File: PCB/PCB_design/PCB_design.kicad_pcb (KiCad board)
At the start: 2 copper layers, 68.2 x 66 mm, 55 parts, among them J1 Conn_01x01_Pin, J2 Conn_01x01_Pin, J3 Conn_01x01_Pin, J4 Conn_01x01_Pin, J5 Conn_01x01_Pin, J6 Conn_01x01_Pin, J7 Conn_02x04_Counter_Clockwise, J8 Conn_01x01_Pin, K1 Relay_SPST-NO, K2 Relay_SPST-NO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

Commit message: Regroupement partie AC
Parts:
- moved J1 50.5 mm to (145.9, 37.9), turned to 180 degrees
- moved J8 35.5 mm to (134.9, 37.6), turned to 180 degrees
- moved R11 32.6 mm to (102.2, 84.4), turned to 0 degrees
- moved F1 32.5 mm to (131.6, 43.9), turned to 180 degrees
- moved J2 31.2 mm to (128.3, 37.6), turned to 180 degrees
- moved R10 27.3 mm to (108.2, 88.7)
- moved R4 26.6 mm to (102.8, 79.8), turned to 180 degrees
- moved C9 24.5 mm to (107.0, 80.8), turned to -90 degrees
- moved R5 22.1 mm to (108.2, 86.2)
- moved U3 20.2 mm to (112.3, 81.8)
- moved R7 19.5 mm to (102.8, 74.5)
- moved D3 18.8 mm to (102.8, 68.5), turned to -90 degrees
- moved C1 18.6 mm to (121.9, 46.0), turned to 90 degrees
- moved C8 17.2 mm to (116.5, 87.9)
- moved D2 17.2 mm to (125.2, 73.9)
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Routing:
- net L: track 251.2 -> 279.2 mm, vias 14 -> 24
- net N: track 41.3 -> 18.3 mm
- net Net-(C1-Pad1): track 38.9 -> 16.3 mm
- net Net-(R11-Pad1): track 1.83 -> 24.3 mm, vias 0 -> 2
- net GND2: track 187.6 -> 208.9 mm, vias 1 -> 2
- net Net-(D1-+): track 14.3 -> 29.7 mm
- net Vaux: track 30.3 -> 16.0 mm
- net Net-(U3-FB): track 9.94 -> 23.5 mm
- net GND: track 109.9 -> 97.2 mm, vias 4 -> 1
- net Net-(D3-K): track 2.84 -> 15.3 mm
- net Net-(D4-A): track 34.5 -> 46.2 mm, vias 0 -> 1
- net VCC_IC: track 7.56 -> 12.3 mm
- net C: track 33.2 -> 34.5 mm
- net +310VDC: track 71.8 -> 70.7 mm, vias 1 -> 0
- net CT2: track 118.9 -> 118.4 mm
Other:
- board size 68.2 x 66 mm -> 64.3 x 77.8 mm

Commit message: J7 femelle
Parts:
- J7: footprint Connector_PinHeader_2.54mm:PinHeader_2x04_P2.54mm_Vertical -> Connector_PinSocket_2.54mm:PinSocket_2x04_P2.54mm_Vertical
- moved J7 2.28 mm to (122.7, 96.8)
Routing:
- net CT2: track 118.4 -> 135.9 mm
- net CT3: track 21.5 -> 27.6 mm, vias 0 -> 1
- net CT1: track 104.8 -> 99.5 mm
- net +5VDC: track 135.4 -> 138.9 mm
- net +3.3V: track 43.2 -> 40.4 mm
- net CT4: track 8.75 -> 6.27 mm
- net GND2: track 208.9 -> 207.3 mm

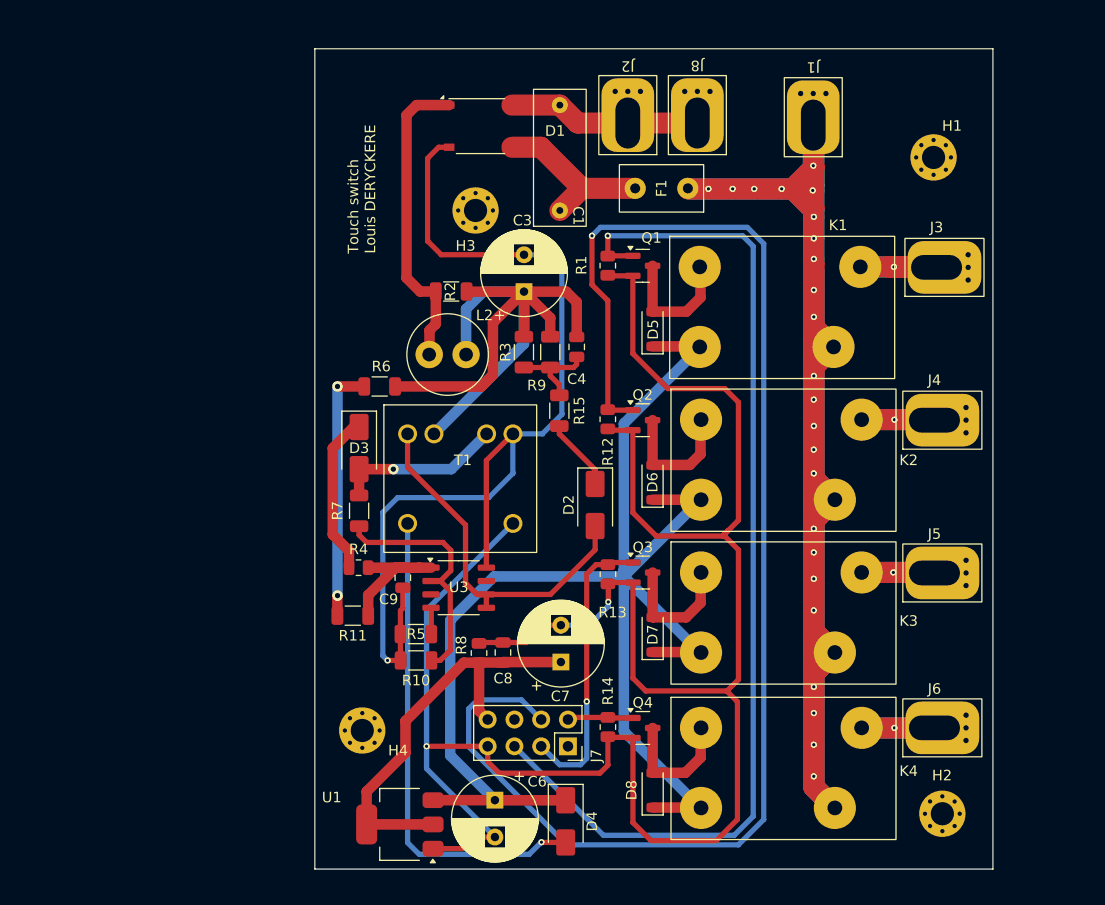
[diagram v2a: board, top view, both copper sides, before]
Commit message: Routage : séparation primaire/secondaire
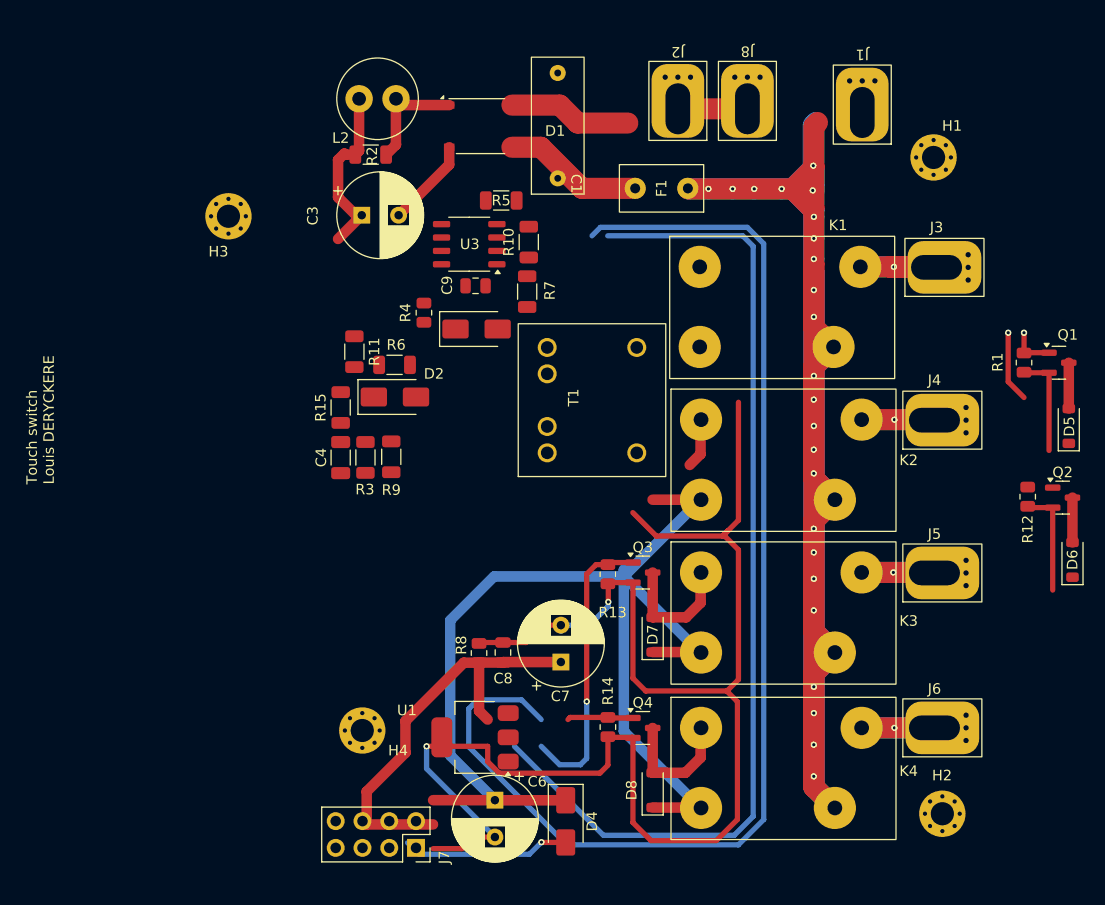
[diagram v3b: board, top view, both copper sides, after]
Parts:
- C4: footprint Capacitor_SMD:C_0805_2012Metric -> Capacitor_SMD:C_1206_3216Metric
- moved R5 41.9 mm to (116.3, 45.0), turned to 180 degrees
- moved R10 41.1 mm to (119.0, 49.0), turned to -90 degrees
- moved D5 40.6 mm to (170.2, 66.4)
- moved Q1 40.6 mm to (169.3, 60.4)
- moved R1 40.6 mm to (165.9, 60.4)
- moved Q2 40.5 mm to (169.6, 73.2)
- moved D6 40.5 mm to (170.6, 79.1)
- moved R12 40.5 mm to (166.3, 73.1)
- moved U3 32.6 mm to (113.3, 49.1), turned to 180 degrees
- moved C9 28.5 mm to (113.9, 53.1), turned to 180 degrees
- moved R7 26.2 mm to (118.8, 53.6), turned to 90 degrees
- moved R11 25.1 mm to (102.4, 59.4), turned to 90 degrees
- moved R4 25.0 mm to (109.0, 55.6), turned to -90 degrees
- moved C4 24.7 mm to (101.1, 69.4), turned to 90 degrees
- moved L2 24.5 mm to (106.3, 35.4), turned to 180 degrees
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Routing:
- net GND: track 97.2 -> 8.44 mm, vias 1 -> 0
- net +310VDC: track 70.7 -> 17.1 mm
- net GND2: track 207.3 -> 170.9 mm
- net C: track 34.5 -> 0.00 mm
- net Net-(D4-A): track 46.2 -> 15.9 mm
- net +5VDC: track 138.9 -> 110.2 mm
- net Net-(R11-Pad1): track 24.3 -> 0.00 mm, vias 2 -> 0
- net Net-(U3-FB): track 23.5 -> 0.00 mm
- net Net-(D1-+): track 29.7 -> 11.0 mm
- net Vaux: track 16.0 -> 0.00 mm, vias 1 -> 0
- net Net-(D3-K): track 15.3 -> 0.00 mm
- net CT2: track 135.9 -> 123.1 mm
- net VCC_IC: track 12.3 -> 0.00 mm
- net Net-(C4-Pad2): track 8.83 -> 0.00 mm
- net Net-(D5-A): track 12.4 -> 4.35 mm
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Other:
- board outline removed

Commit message: Routage
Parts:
- moved Q2 41.4 mm to (128.6, 79.2)
- moved Q1 41.4 mm to (128.4, 53.6)
- moved R12 41.3 mm to (125.5, 79.2)
- moved D5 40.1 mm to (131.7, 55.2)
- moved D6 38.7 mm to (131.8, 79.8)
- moved R1 37.5 mm to (128.6, 56.6), turned to 180 degrees
- moved H3 28.7 mm to (115.5, 32.5)
- moved C6 24.6 mm to (108.8, 78.3), turned to 0 degrees
- moved D4 22.9 mm to (119.8, 81.2), turned to 0 degrees
- moved J7 16.3 mm to (103.2, 90.9), turned to 0 degrees
- moved C7 12.5 mm to (111.2, 95.0), turned to -90 degrees
- moved H4 9.70 mm to (100.4, 104.6)
- moved U1 8.89 mm to (111.1, 87.5), turned to -90 degrees
- moved R8 6.95 mm to (119.2, 92.8), turned to 90 degrees
- moved Q3 5.83 mm to (128.5, 86.0)
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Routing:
- net CT2: track 123.1 -> 39.1 mm
- net GND2: track 170.9 -> 101.3 mm, vias 2 -> 4
- net GND: track 8.44 -> 63.8 mm, vias 0 -> 1
- net L: track 279.2 -> 225.5 mm, vias 24 -> 21
- net +310VDC: track 17.1 -> 58.5 mm, vias 0 -> 2
- net C: track 0.00 -> 38.8 mm, vias 0 -> 2
- net CT4: track 6.27 -> 35.4 mm, vias 0 -> 1
- net VCC_IC: track 0.00 -> 18.8 mm
- net CT1: track 99.5 -> 117.2 mm
- net Vaux: track 0.00 -> 11.9 mm
- net +3.3V: track 40.4 -> 52.0 mm
- net +5VDC: track 110.2 -> 120.0 mm, vias 0 -> 7
- net CT3: track 27.6 -> 35.8 mm
- net Net-(D6-A): track 8.98 -> 15.8 mm
- net Net-(D3-K): track 0.00 -> 6.73 mm
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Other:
- board outline added: 67.4 x 80 mm

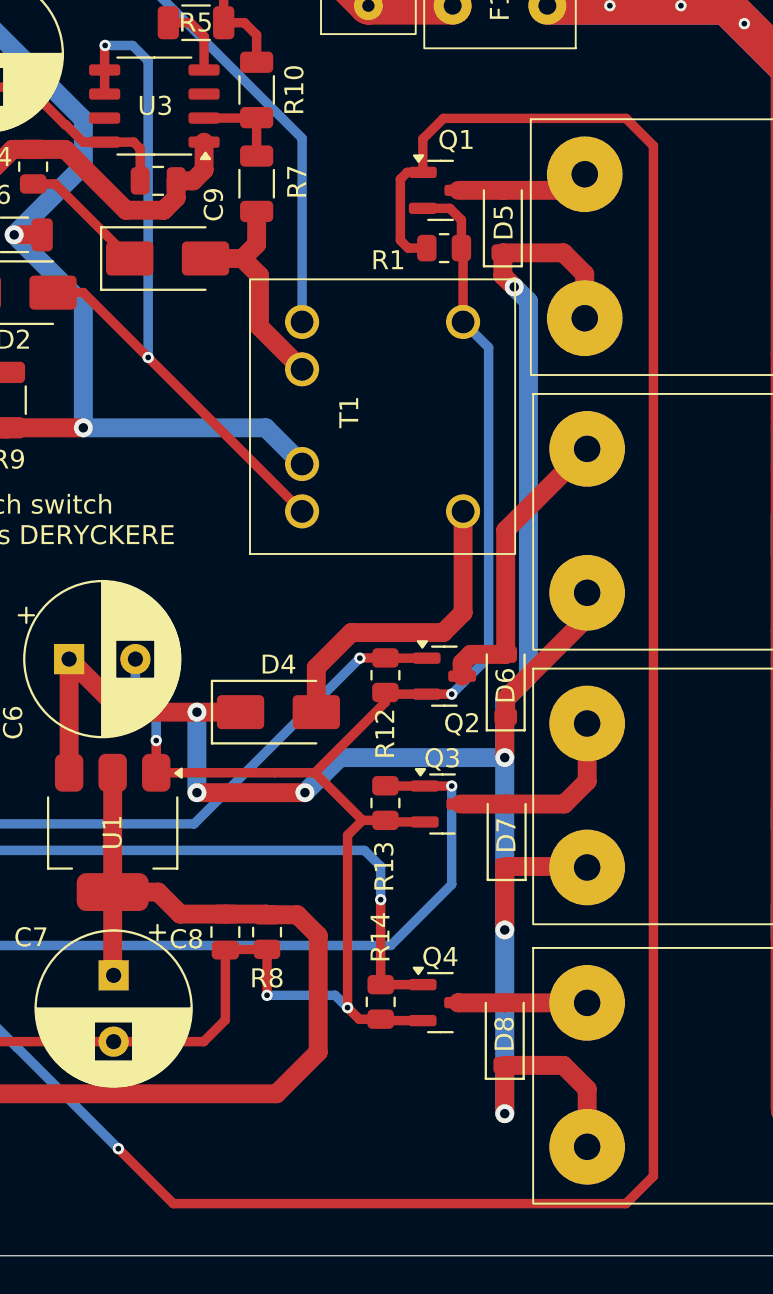
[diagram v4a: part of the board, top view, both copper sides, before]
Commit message: Rédaction README
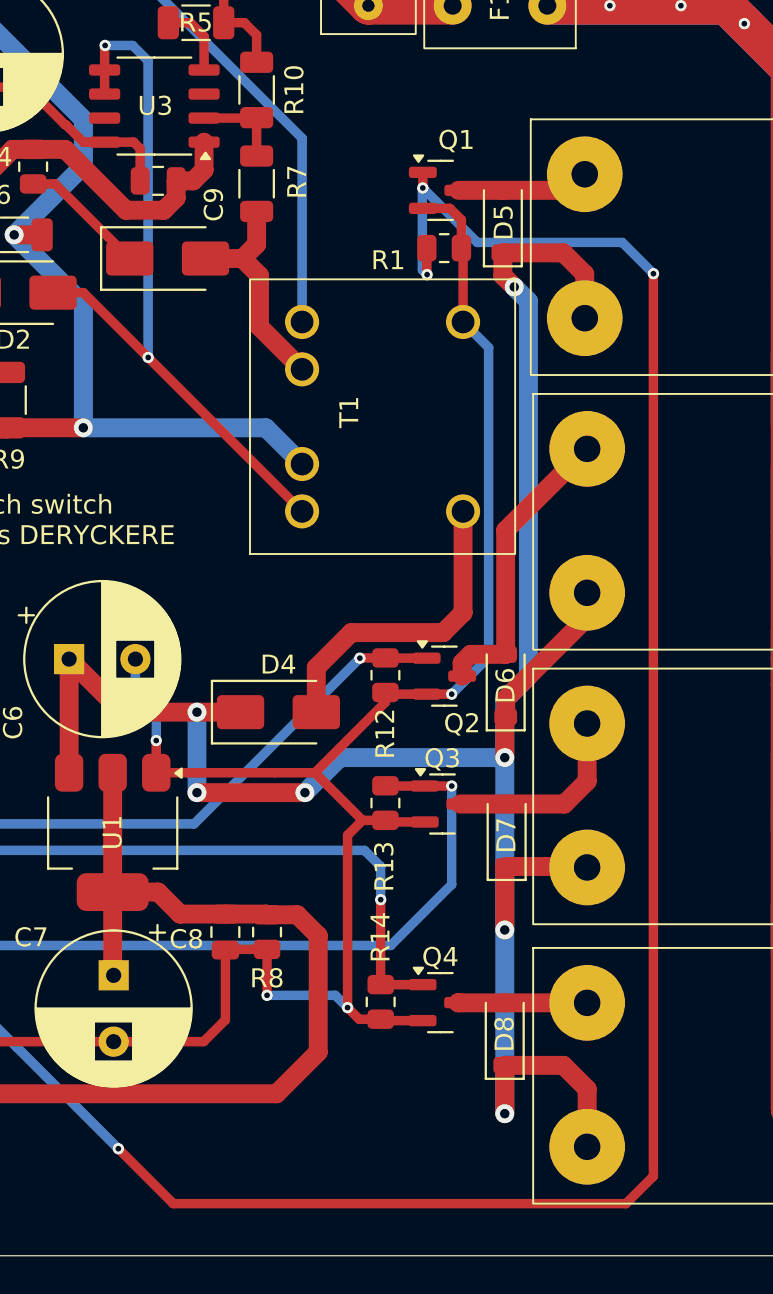
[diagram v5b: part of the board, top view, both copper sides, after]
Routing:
- net CT1: track 117.2 -> 110.3 mm, vias 1 -> 4
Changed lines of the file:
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@@
 		(tags "capacitor")
 		(property "Reference" "C8"
-			(at -0.3875 -2.05 360)
+			(at -0.3875 -2.05 0)
 			(layer "F.SilkS")
 			(effects
@@
 		)
 		(property "Value" "0,1u/10V"
-			(at 0 1.68 270)
+			(at 0 1.68 -90)
 			(layer "F.Fab")
 			(effects
@@
 		)
 		(fp_text user "${REFERENCE}"
-			(at 0 0 270)
+			(at 0 0 -90)
 			(layer "F.Fab")
 			(effects
@@
 		(tags "resistor")
 		(property "Reference" "R15"
-			(at 0 -1.9 270)
+			(at 0 -1.9 -90)
 			(layer "F.SilkS")
 			(effects
@@
 		)
 		(property "Value" "100"
-			(at 0 1.82 270)
+			(at 0 1.82 -90)
 			(layer "F.Fab")
 			(effects
@@
 		)
 		(fp_text user "${REFERENCE}"
-			(at 0 0 270)
+			(at 0 0 -90)
 			(layer "F.Fab")
 			(effects
@@
 		(tags "Diode SMA (DO-214AC)")
 		(property "Reference" "D2"
-			(at -0.1 2.5 360)
+			(at -0.1 2.5 0)
 			(layer "F.SilkS")
 			(effects
@@
 		)
 		(property "Value" "D"
-			(at 0 2.6 360)
+			(at 0 2.6 0)
 			(layer "F.Fab")
 			(effects
@@
 		)
 		(fp_text user "${REFERENCE}"
-			(at 0 -2.5 360)
+			(at 0 -2.5 0)
 			(layer "F.Fab")
 			(effects
@@
 		(tags "resistor")
 		(property "Reference" "R9"
-			(at -3.15 0 360)
+			(at -3.15 0 0)
 			(layer "F.SilkS")
 			(effects
@@
 		)
 		(property "Value" "430k"
-			(at 0 1.82 270)
+			(at 0 1.82 -90)
 			(layer "F.Fab")
 			(effects
@@
 		)
 		(fp_text user "${REFERENCE}"
-			(at 0 0 270)
+			(at 0 0 -90)
 			(layer "F.Fab")
 			(effects
@@
 		)
 		(property "Value" "D"
-			(at 0 2.6 360)
+			(at 0 2.6 0)
 			(layer "F.Fab")
 			(effects
@@
 		)
 		(fp_text user "${REFERENCE}"
-			(at 0 -2.5 360)
+			(at 0 -2.5 0)
 			(layer "F.Fab")
 			(effects
@@
 		(tags "Through hole socket strip THT 2x04 2.54mm double row")
 		(property "Reference" "J7"
-			(at 0.9 -2.68 360)
+			(at 0.9 -2.68 0)
 			(layer "F.SilkS")
 			(effects
@@
 		)
 		(property "Value" "Conn_02x04_Counter_Clockwise"
-			(at -1.27 10.39 360)
+			(at -1.27 10.39 0)
 			(layer "F.Fab")
 			(effects
@@
 		)
 		(property "Value" "430k"
-			(at 0 1.82 270)
+			(at 0 1.82 -90)
 			(layer "F.Fab")
 			(effects
@@
 		)
 		(fp_text user "${REFERENCE}"
-			(at 0 0 270)
+			(at 0 0 -90)
 			(layer "F.Fab")
 			(effects
@@
 		(tags "resistor")
 		(property "Reference" "R7"
-			(at 0.1 2.15 270)
+			(at 0.1 2.15 -90)
 			(layer "F.SilkS")
 			(effects
@@
 		)
 		(property "Value" "24k"
-			(at 0 1.82 270)
+			(at 0 1.82 -90)
 			(layer "F.Fab")
 			(effects
@@
 		)
 		(fp_text user "${REFERENCE}"
-			(at 0 0 270)
+			(at 0 0 -90)
 			(layer "F.Fab")
 			(effects
@@
 		(tags "resistor")
 		(property "Reference" "R11"
-			(at 0 -2 270)
+			(at 0 -2 -90)
 			(layer "F.SilkS")
 			(effects
@@
 		)
 		(property "Value" "2M"
-			(at 0 1.82 270)
+			(at 0 1.82 -90)
 			(layer "F.Fab")
 			(effects
@@
 		)
 		(fp_text user "${REFERENCE}"
-			(at 0 0 270)
+			(at 0 0 -90)
 			(layer "F.Fab")
 			(effects
@@
 		(tags "resistor")
 		(property "Reference" "R8"
-			(at -2.45 0 360)
+			(at -2.45 0 0)
 			(layer "F.SilkS")
 			(effects
@@
 		)
 		(property "Value" "1k"
-			(at 0 1.65 270)
+			(at 0 1.65 -90)
 			(layer "F.Fab")
 			(effects
@@
 		)
 		(fp_text user "${REFERENCE}"
-			(at 0 0 270)
+			(at 0 0 -90)
 			(layer "F.Fab")
 			(effects
@@
 		(tags "capacitor")
 		(property "Reference" "C4"
-			(at 0 -1.85 270)
+			(at 0 -1.85 -90)
 			(layer "F.SilkS")
 			(effects
@@
 		)
 		(property "Value" "100p/400V"
-			(at 0 1.85 270)
+			(at 0 1.85 -90)
 			(layer "F.Fab")
 			(effects
@@
 		)
 		(fp_text user "${REFERENCE}"
-			(at 0 0 270)
+			(at 0 0 -90)
 			(layer "F.Fab")
 			(effects
@@
 		(tags "Diode SMA (DO-214AC)")
 		(property "Reference" "D4"
-			(at 0 -2.5 360)
+			(at 0 -2.5 0)
 			(layer "F.SilkS")
 			(effects
@@
 		)
 		(property "Value" "D"
-			(at 0 2.6 360)
+			(at 0 2.6 0)
 			(layer "F.Fab")
 			(effects
@@
 		)
 		(fp_text user "${REFERENCE}"
-			(at 0 -2.5 360)
+			(at 0 -2.5 0)
 			(layer "F.Fab")
 			(effects
@@
 		(tags "ABS MBLS")
 		(property "Reference" "D1"
-			(at 0 0 360)
+			(at 0 0 0)
 			(layer "F.SilkS")
 			(effects
@@
 		)
 		(property "Value" "D_Bridge_+-AA"
-			(at 0 3.7 360)
+			(at 0 3.7 0)
 			(layer "F.Fab")
 			(effects
@@
 		)
 		(fp_text user "${REFERENCE}"
-			(at 0 -0.065 360)
+			(at 0 -0.065 0)
 			(layer "F.Fab")
 			(effects
@@
 		(tags "capacitor")
 		(property "Reference" "C9"
-			(at -2.95 -1.25 270)
+			(at -2.95 -1.25 -90)
 			(layer "F.SilkS")
 			(effects
@@
 		)
 		(property "Value" "470u/10V"
-			(at 1.75 5.25 360)
+			(at 1.75 5.25 0)
 			(layer "F.Fab")
 			(effects
@@
 		)
 		(fp_text user "${REFERENCE}"
-			(at 1.75 0 360)
+			(at 1.75 0 0)
 			(layer "F.Fab")
 			(effects
@@
 	)
 	(segment
-		(start 138.2 49.8)
-		(end 128.5625 49.8)
+		(start 127.6875 56.65)
+		(end 127.6875 58.0375)
 		(width 0.5)
 		(layer "F.Cu")
@@
 	)
 	(segment
-		(start 128.5625 49.8)
-		(end 127.475 50.8875)
+		(start 139.65 58)
+		(end 139.65 105.65)
 		(width 0.5)
 		(layer "F.Cu")
@@
 	)
 	(segment
-		(start 126.65 52.65)
-		(end 127.475 52.65)
+		(start 139.65 105.65)
+		(end 138.2 107.1)
 		(width 0.5)
 		(layer "F.Cu")
@@
 	)
 	(segment
-		(start 139.65 51.25)
-		(end 138.2 49.8)
+		(start 138.2 107.1)
+		(end 114.3 107.1)
 		(width 0.5)
 		(layer "F.Cu")
@@
 	)
 	(segment
-		(start 138.2 107.1)
-		(end 139.65 105.65)
+		(start 114.3 107.1)
+		(end 111.4 104.2)
 		(width 0.5)
 		(layer "F.Cu")
@@
 	)
 	(segment
-		(start 139.65 105.65)
-		(end 139.65 51.25)
+		(start 127.475 53.475)
+		(end 127.475 52.65)
 		(width 0.5)
 		(layer "F.Cu")
@@
 	)
 	(segment
-		(start 127.6875 56.65)
-		(end 126.7 56.65)
+		(start 127.6875 58.0375)
+		(end 127.7 58.05)
 		(width 0.5)
 		(layer "F.Cu")
 		(net 18)
 	)
-	(segment
-		(start 127.475 50.8875)
-		(end 127.475 52.65)
-		(width 0.5)
-		(layer "F.Cu")
+	(via
+		(at 127.7 58.05)
+		(size 0.6)
+		(drill 0.3)
+		(layers "F.Cu" "B.Cu")
 		(net 18)
 	)
-	(segment
-		(start 111.4 104.2)
-		(end 114.3 107.1)
-		(width 0.5)
-		(layer "F.Cu")
+	(via
+		(at 127.475 53.475)
+		(size 0.6)
+		(drill 0.3)
+		(layers "F.Cu" "B.Cu")
+		(net 18)
+	)
+	(via
+		(at 139.65 58)
+		(size 0.6)
+		(drill 0.3)
+		(layers "F.Cu" "B.Cu")
+		(net 18)
+	)
+	(via
+		(at 111.4 104.2)
+		(size 0.6)
+		(drill 0.3)
+		(layers "F.Cu" "B.Cu")
 		(net 18)
 	)
 	(segment
-		(start 114.3 107.1)
-		(end 138.2 107.1)
+		(start 130.35 56.35)
+		(end 138 56.35)
 		(width 0.5)
-		(layer "F.Cu")
+		(layer "B.Cu")
 		(net 18)
 	)
 	(segment
-		(start 126.2875 53.0125)
-		(end 126.65 52.65)
+		(start 106.05 98.86)
+		(end 103.2 96.01)
 		(width 0.5)
-		(layer "F.Cu")
+		(layer "B.Cu")
 		(net 18)
 	)
 	(segment
-		(start 126.2875 56.2375)
-		(end 126.2875 53.0125)
+		(start 127.45 53.5)
+		(end 127.45 57.8)
 		(width 0.5)
-		(layer "F.Cu")
+		(layer "B.Cu")
 		(net 18)
 	)
 	(segment
-		(start 126.7 56.65)
-		(end 126.2875 56.2375)
+		(start 111.4 104.2)
+		(end 106.06 98.86)
 		(width 0.5)
-		(layer "F.Cu")
+		(layer "B.Cu")
 		(net 18)
 	)
-	(via
-		(at 111.4 104.2)
-		(size 0.6)
-		(drill 0.3)
-		(layers "F.Cu" "B.Cu")
+	(segment
+		(start 127.475 53.475)
+		(end 130.35 56.35)
+		(width 0.5)
+		(layer "B.Cu")
 		(net 18)
 	)
 	(segment
-		(start 106.05 98.86)
-		(end 103.2 96.01)
+		(start 138 56.35)
+		(end 139.65 58)
 		(width 0.5)
 		(layer "B.Cu")
@@
 	)
 	(segment
-		(start 111.4 104.2)
-		(end 106.06 98.86)
+		(start 127.475 53.475)
+		(end 127.45 53.5)
 		(width 0.5)
 		(layer "B.Cu")
@@
 		(width 0.5)
 		(layer "B.Cu")
+		(net 18)
+	)
+	(segment
+		(start 127.45 57.8)
+		(end 127.7 58.05)
+		(width 0.5)
+		(layer "B.Cu")
